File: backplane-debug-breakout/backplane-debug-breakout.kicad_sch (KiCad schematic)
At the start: 20 parts, among them J1 Conn_02x08_Odd_Even, J2 Conn_01x04, J4 Conn_01x02_Socket, J5 Conn_01x04, J6 629105150521, SW1 SW_Push_DPDT, SW2 SW_Omron_B3FS, SW3 EG1218, U1 UMFT234XF

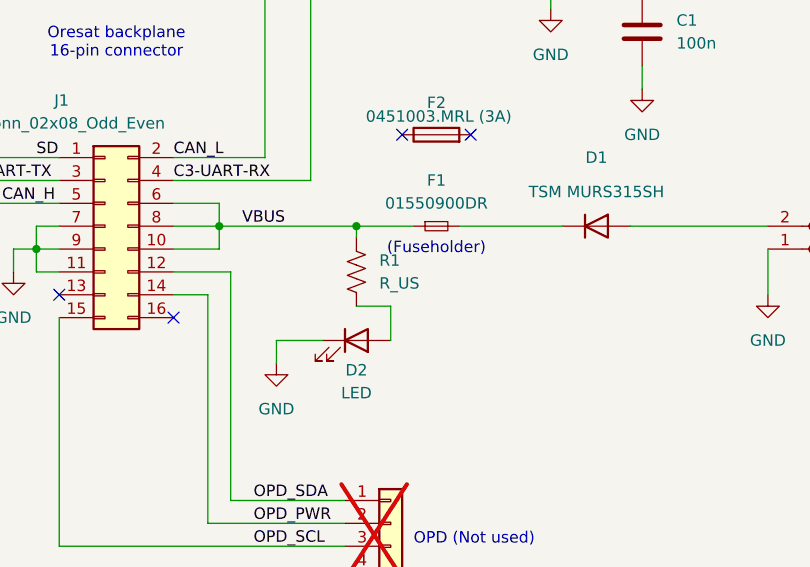
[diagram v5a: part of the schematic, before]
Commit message: chose DPDT for backplane debug breakout and finished BOM
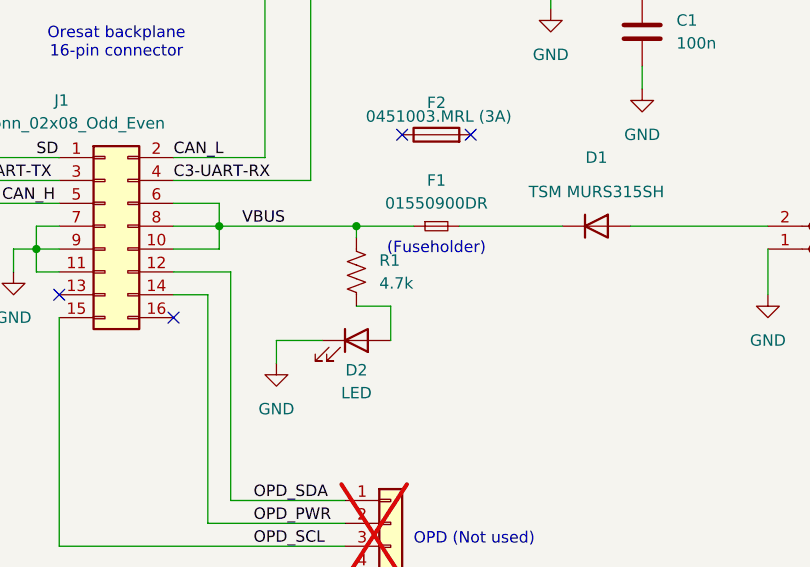
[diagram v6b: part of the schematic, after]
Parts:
- C1: DPN (none) -> 587-3472-1-ND; DST (none) -> Digi-Key; MFR (none) -> Taiyo Yuden; MPN (none) -> TMK107BJ104KAHT
- D2: DPN (none) -> 732-4978-1-ND; DST (none) -> Digi-Key; MFR (none) -> Wurth; MPN (none) -> 150060RS75000
- R1: value R_US -> 4.7k; DPN (none) -> RMCF0603FT4K70CT-ND; DST (none) -> Digi-Key; MFR (none) -> Stackpole Electronics Inc; MPN (none) -> RMCF0603FT4K70
- SW1: footprint oresat-passives:DPDT slide switch 6 pin -> oresat-passives:EG2209 DPDT; DPN (none) -> EG1907-ND; DST (none) -> Digi-Key; MFR (none) -> E-Switch; MPN (none) -> EG2209
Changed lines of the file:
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@@
 			)
 		)
-		(property "Footprint" "oresat-passives:DPDT slide switch 6 pin"
+		(property "Footprint" "oresat-passives:EG2209 DPDT"
 			(at 135.89 59.69 0)
 			(effects
@@
 		)
 		(property "Description" "Momentary Switch, dual pole double throw"
+			(at 140.97 59.69 0)
+			(effects
+				(font
+					(size 1.27 1.27)
+				)
+				(hide yes)
+			)
+		)
+		(property "DPN" "EG1907-ND"
+			(at 140.97 59.69 0)
+			(effects
+				(font
+					(size 1.27 1.27)
+				)
+				(hide yes)
+			)
+		)
+		(property "DST" "Digi-Key"
+			(at 140.97 59.69 0)
+			(effects
+				(font
+					(size 1.27 1.27)
+				)
+				(hide yes)
+			)
+		)
+		(property "MFR" "E-Switch"
+			(at 140.97 59.69 0)
+			(effects
+				(font
+					(size 1.27 1.27)
+				)
+				(hide yes)
+			)
+		)
+		(property "MPN" "EG2209"
 			(at 140.97 59.69 0)
 			(effects
@@
 			)
 		)
+		(property "DPN" "587-3472-1-ND"
+			(at 204.47 76.2 0)
+			(effects
+				(font
+					(size 1.27 1.27)
+				)
+				(hide yes)
+			)
+		)
+		(property "DST" "Digi-Key"
+			(at 204.47 76.2 0)
+			(effects
+				(font
+					(size 1.27 1.27)
+				)
+				(hide yes)
+			)
+		)
+		(property "MFR" "Taiyo Yuden"
+			(at 204.47 76.2 0)
+			(effects
+				(font
+					(size 1.27 1.27)
+				)
+				(hide yes)
+			)
+		)
+		(property "MPN" "TMK107BJ104KAHT"
+			(at 204.47 76.2 0)
+			(effects
+				(font
+					(size 1.27 1.27)
+				)
+				(hide yes)
+			)
+		)
 		(pin "1"
 		)
@@
 			)
 		)
+		(property "DPN" "732-4978-1-ND"
+			(at 172.72 110.49 0)
+			(effects
+				(font
+					(size 1.27 1.27)
+				)
+				(hide yes)
+			)
+		)
+		(property "DST" "Digi-Key"
+			(at 172.72 110.49 0)
+			(effects
+				(font
+					(size 1.27 1.27)
+				)
+				(hide yes)
+			)
+		)
+		(property "MFR" "Wurth"
+			(at 172.72 110.49 0)
+			(effects
+				(font
+					(size 1.27 1.27)
+				)
+				(hide yes)
+			)
+		)
+		(property "MPN" "150060RS75000"
+			(at 172.72 110.49 0)
+			(effects
+				(font
+					(size 1.27 1.27)
+				)
+				(hide yes)
+			)
+		)
 		(pin "1"
 		)
@@
 			)
 		)
-		(property "Value" "R_US"
+		(property "Value" "4.7k"
 			(at 175.26 104.1399 0)
 			(effects
@@
 			(at 172.72 102.87 0)
 			(effects
+				(font
+					(size 1.27 1.27)
+				)
+				(hide yes)
+			)
+		)
+		(property "DPN" "RMCF0603FT4K70CT-ND"
+			(at 172.72 102.87 0)
+			(effects
+				(font
+					(size 1.27 1.27)
+				)
+				(hide yes)
+			)
+		)
+		(property "DST" "Digi-Key"
+			(at 172.72 102.87 0)
+			(effects
+				(font
+					(size 1.27 1.27)
+				)
+				(hide yes)
+			)
+		)
+		(property "MFR" "Stackpole Electronics Inc"
+			(at 172.72 102.87 0)
+			(effects
+				(font
+					(size 1.27 1.27)
+				)
+				(hide yes)
+			)
+		)
+		(property "MPN" "RMCF0603FT4K70"
+			(at 172.72 102.87 0)
+			(effects

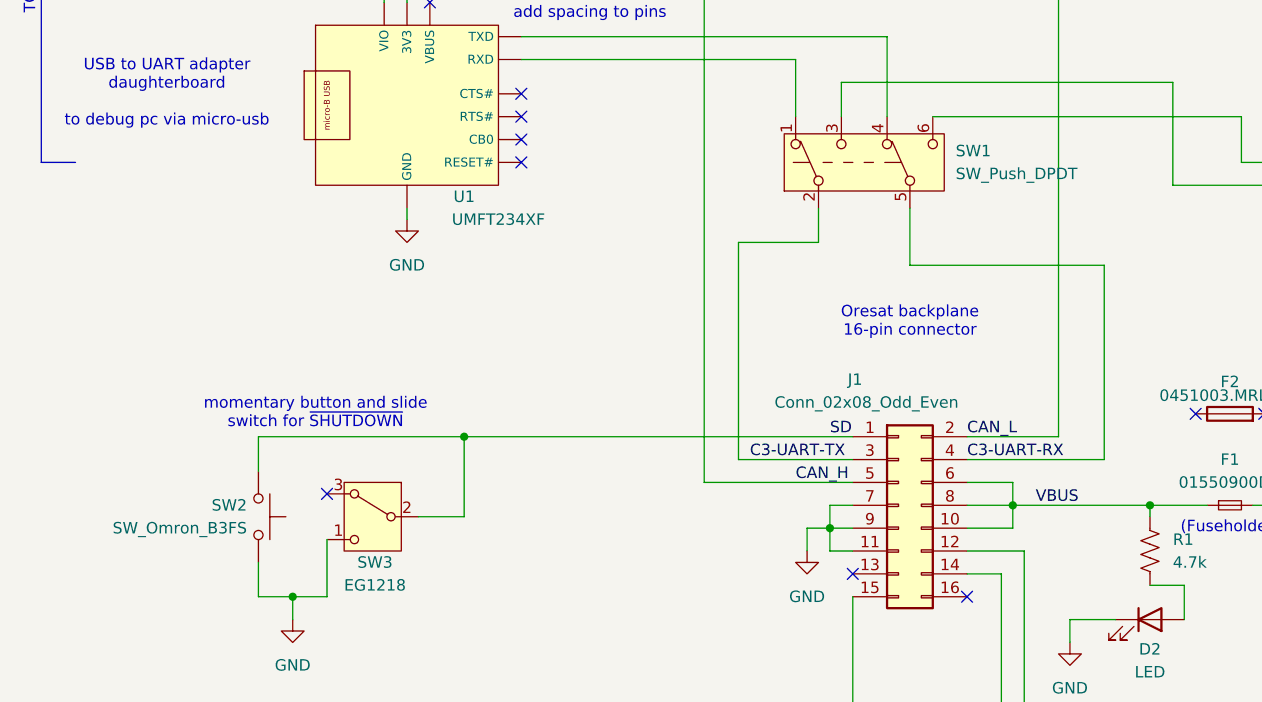
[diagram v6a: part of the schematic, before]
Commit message: Changes generic values on switches to mfgr part number. Re-ran ERC and DRC, made vulcan adapter to be PCB only, and updated to 8.0.7.
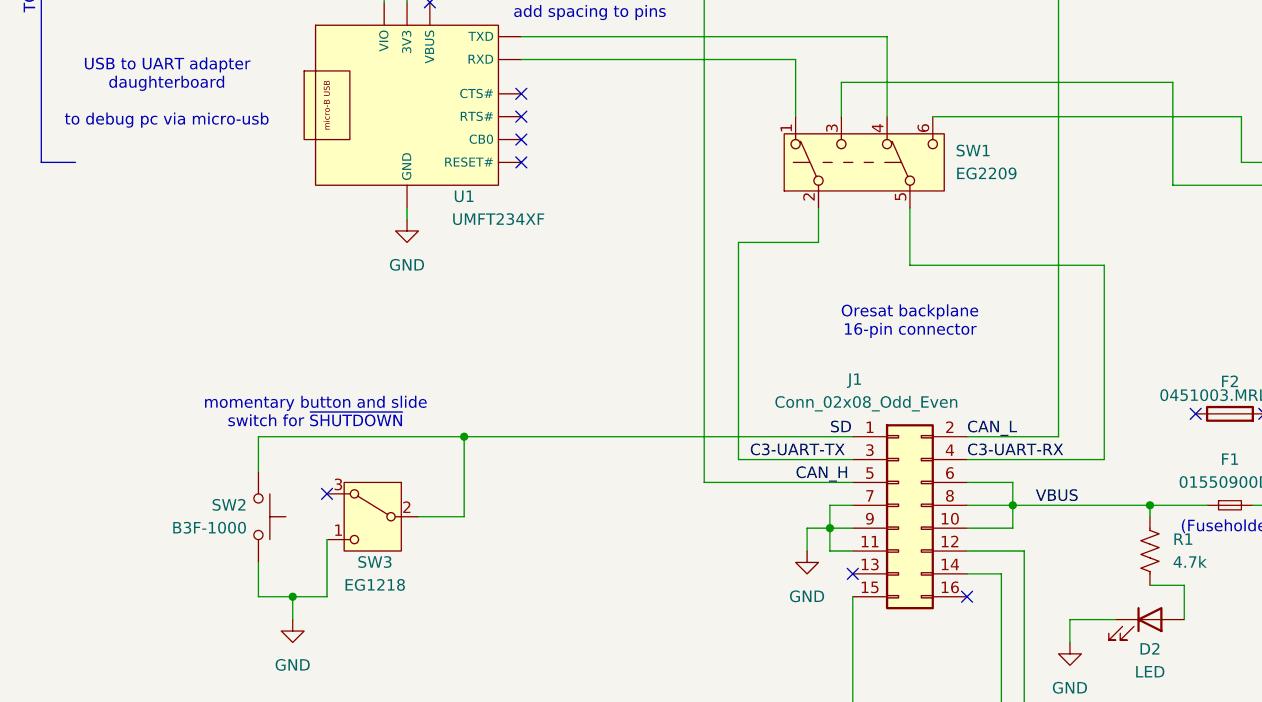
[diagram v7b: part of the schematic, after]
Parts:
- SW1: value SW_Push_DPDT -> EG2209
- SW2: value SW_Omron_B3FS -> B3F-1000
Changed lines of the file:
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@@
 			)
 		)
-		(property "Value" "SW_Push_DPDT"
+		(property "Value" "EG2209"
 			(at 151.13 60.9599 90)
 			(effects
@@
 			)
 		)
-		(property "Value" "SW_Omron_B3FS"
+		(property "Value" "B3F-1000"
 			(at 72.39 100.3299 90)
 			(effects
